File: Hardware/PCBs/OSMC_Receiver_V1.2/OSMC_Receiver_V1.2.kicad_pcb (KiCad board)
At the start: 4 copper layers, 120.7 x 78.7 mm, 115 parts, among them J1 Conn_01x04, J10 Conn_01x04, J11 Conn_01x04, J12 Conn_01x04, J13 Conn_01x04, J14 Conn_01x04, J15 Conn_01x04, J16 Conn_01x04, J2 Conn_01x04, J3 Conn_01x04, J4 Conn_01x04, J5 Conn_01x04, J6 Conn_01x04, J7 Conn_01x04, J8 Conn_01x04, J9 Conn_01x04, U1 24AA02-OT, U13 OSMC Module Board, U14 OSMC Module Board, U15 OSMC Module Board, U16 OSMC Module Board, U17 OSMC Module Board, U18 OSMC Module Board, U19 OSMC Module Board, U2 LTC4317, U20 OSMC Module Board, U3 XIAO-ESP32-S3-DIP, U4 PCF8574DWR, U5 LTC4317, U6 LTC4317, U7 LTC4317

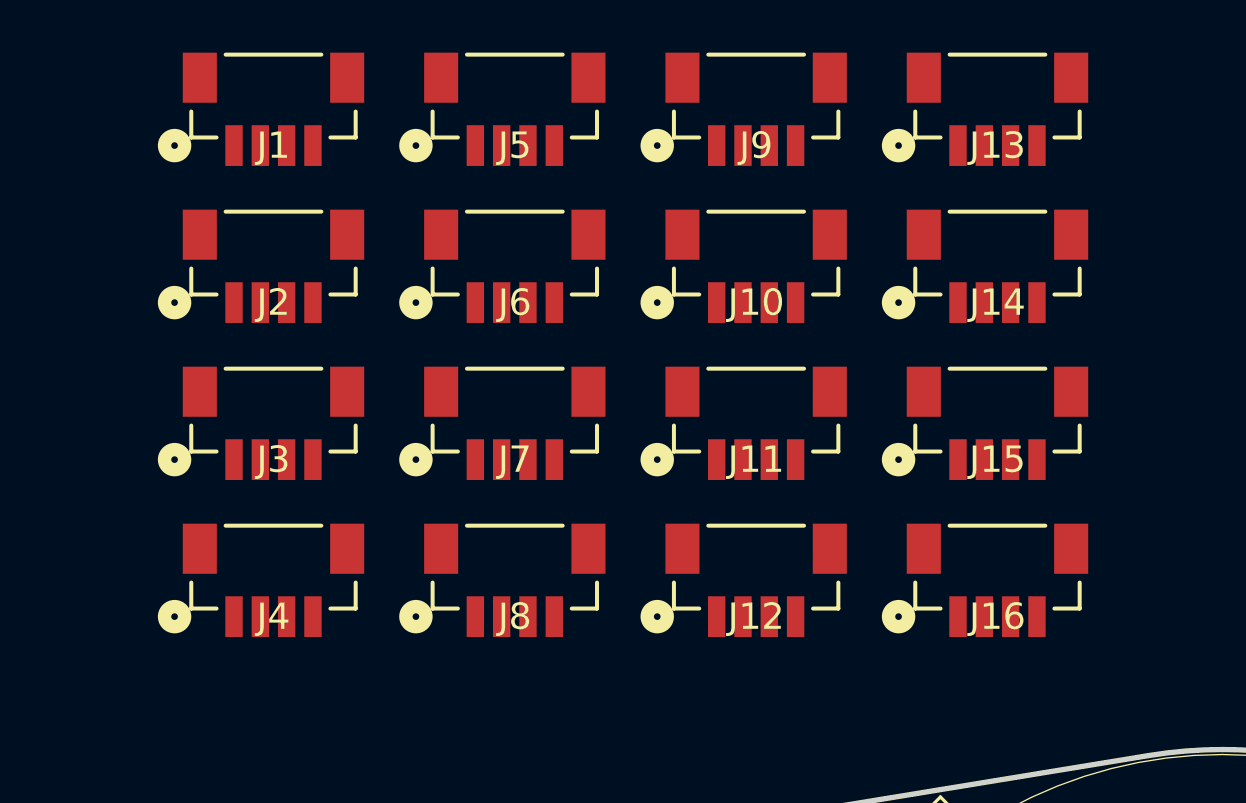
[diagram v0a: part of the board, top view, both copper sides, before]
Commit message: removed redundent connectors
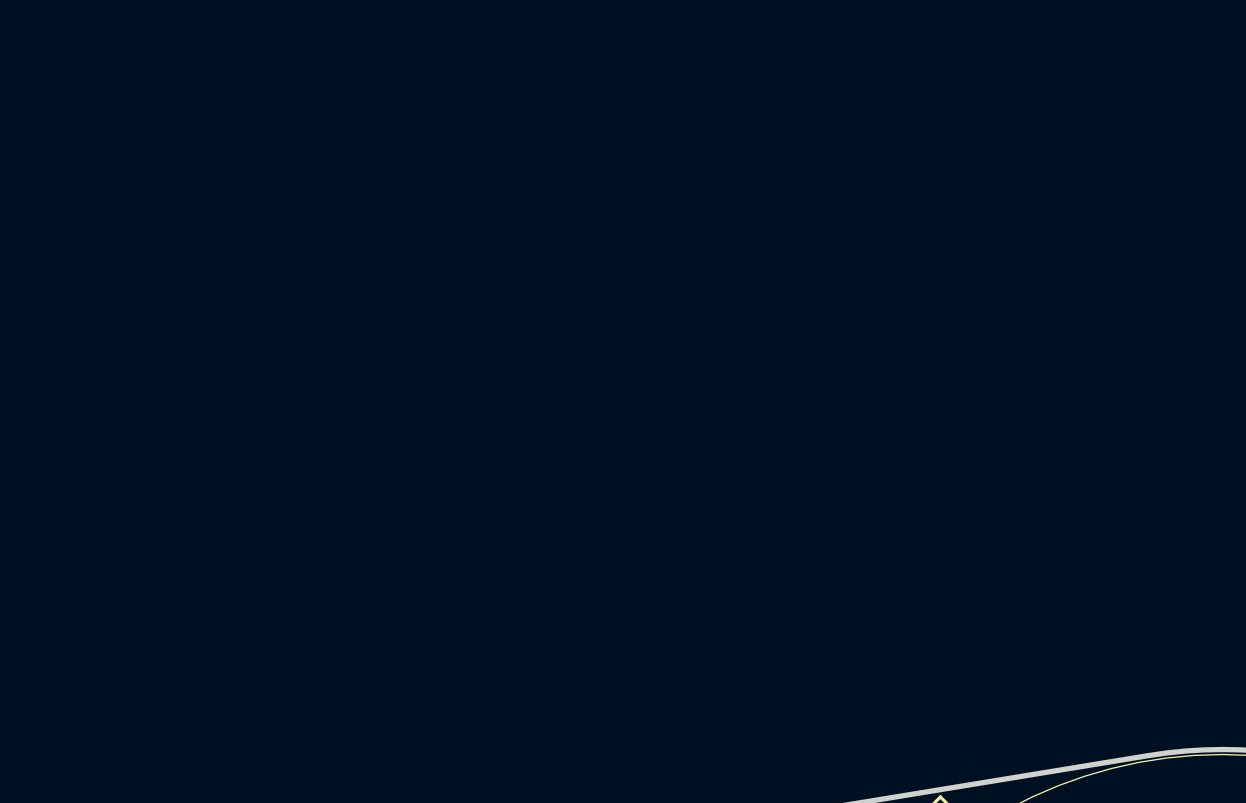
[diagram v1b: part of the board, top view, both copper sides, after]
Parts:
- removed J1, J10, J11, J12, J13, J14, J15, J16, J2, J3, J4, J5, J6, J7, J8, J9: Conn_01x04, OSMC_Module:CONN4_BM04B-SRSS_JST
